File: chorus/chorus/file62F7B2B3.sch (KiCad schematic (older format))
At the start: 14 parts, among them J2 ISP, U1 LM13700, U3 ATTINY85

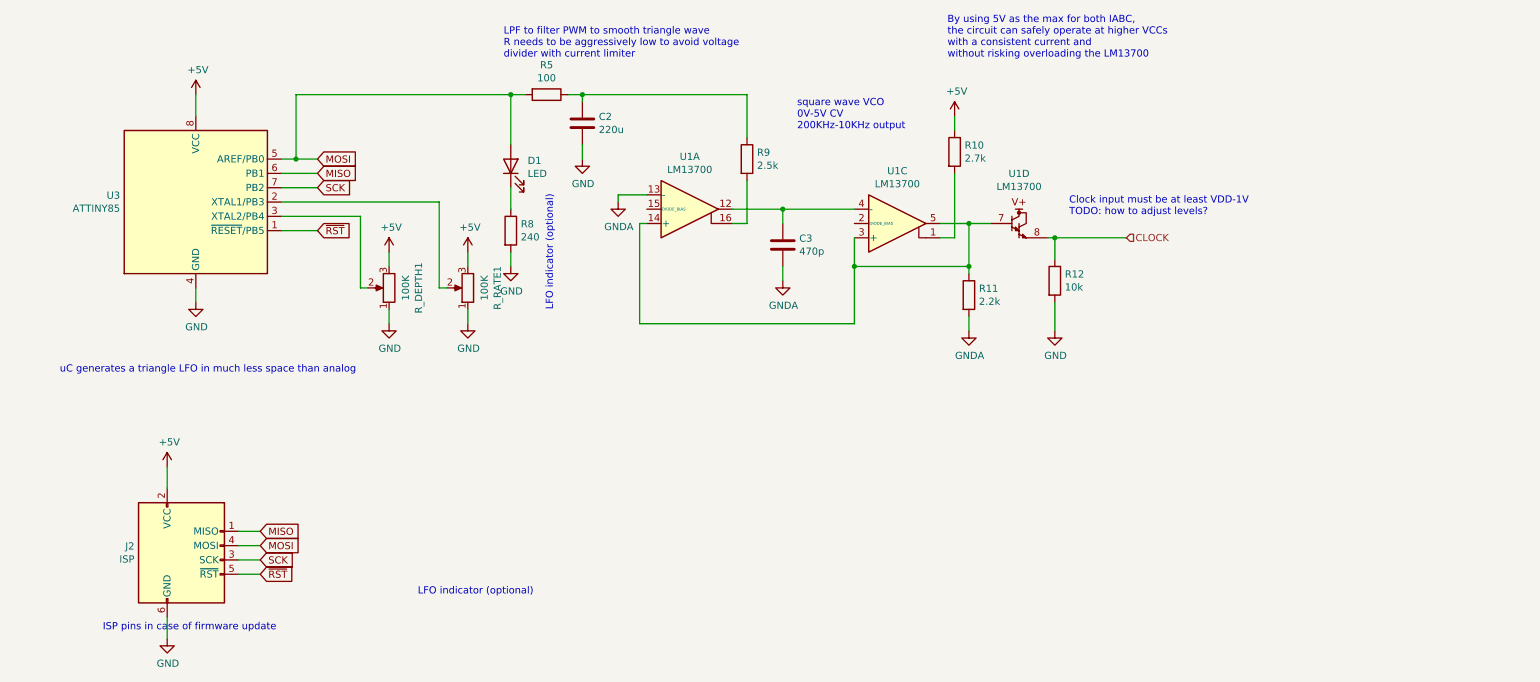
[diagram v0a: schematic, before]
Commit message: add wet/dry mix and recalculate filters
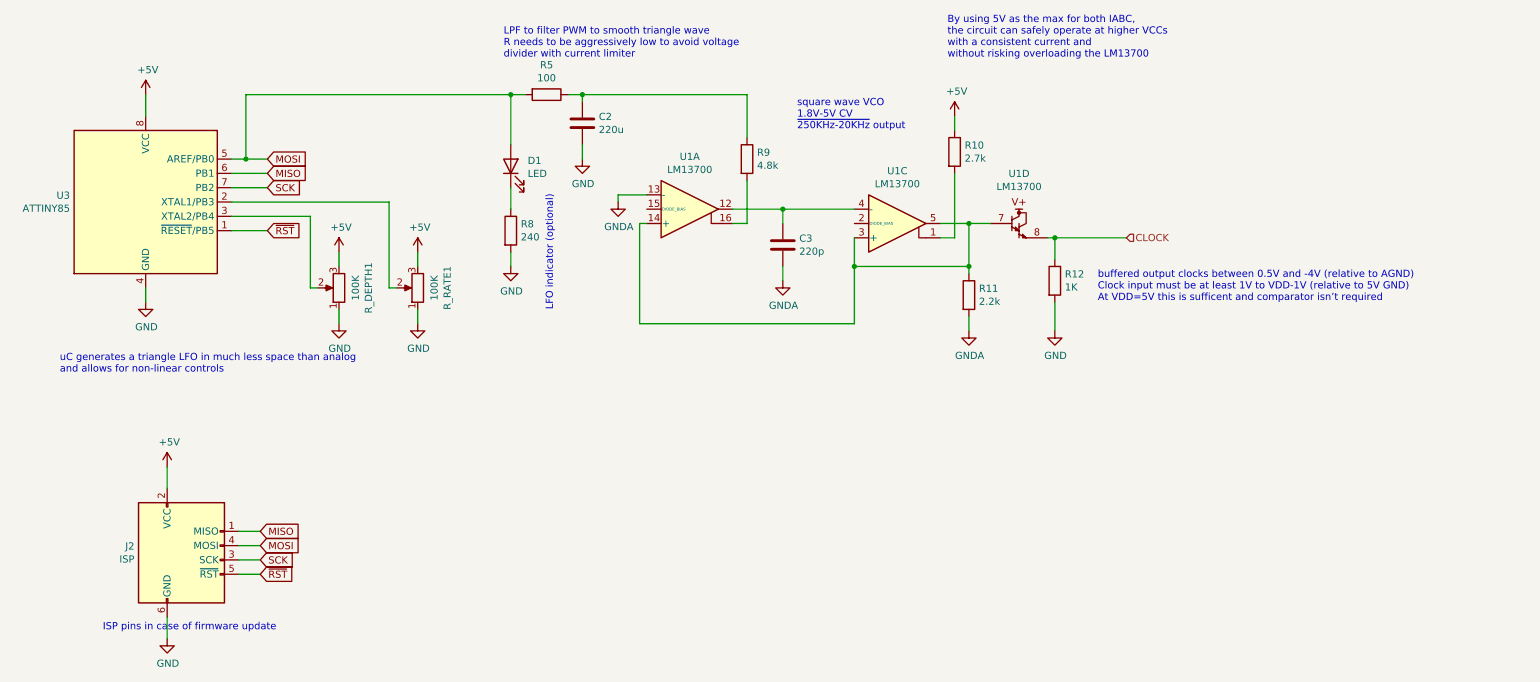
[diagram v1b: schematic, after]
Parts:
- C3: value 470p -> 220p
- R12: value 10k -> 1K
- R9: value 2.5k -> 4.8k
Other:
- note added: "buffered output clocks between 0.5V and -4V (relative to AGND)\nClock input must be at least 1V to VDD-1V (relative to 5V GND)\nAt VDD=5V this is sufficent and comparator isn’t required"
- note added: "square wave VCO\n1.8V-5V CV\n~250KHz-20KHz output"
- note added: "uC generates a triangle LFO in much less space than analog\nand allows for non-linear controls"
- note removed: "Clock input must be at least VDD-1V\nTODO: how to adjust levels?"
- note removed: "square wave VCO\n0V-5V CV\n200KHz-10KHz output"
- note removed: "uC generates a triangle LFO in much less space than analog"
- moved on the sheet: R_DEPTH1, R_RATE1, U3
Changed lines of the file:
@@
 $Descr A4 11693 8268
 encoding utf-8
-Sheet 4 6
+Sheet 3 6
 Title ""
 Date ""
@@
 L MCU_Microchip_ATtiny:ATtiny85-20PU U?
 U 1 1 62F9D27C
-P 1750 3600
+P 1400 3600
 AR Path="/62F9D27C" Ref="U?"  Part="1"
 AR Path="/62F7B2B4/62F9D27C" Ref="U3"  Part="1"
-F 0 "U3" H 1221 3646 50  0000 R CNN
-F 1 "ATTINY85" H 1221 3555 50  0000 R CNN
-F 2 "Package_DIP:DIP-8_W7.62mm" H 1750 3600 50  0001 C CIN
-F 3 "http://www.ti.com/lit/ds/symlink/tl071.pdf" H 1750 3600 50  0001 C CNN
-	1    1750 3600
+F 0 "U3" H 871 3646 50  0000 R CNN
+F 1 "ATTINY85" H 871 3555 50  0000 R CNN
+F 2 "Package_DIP:DIP-8_W7.62mm" H 1400 3600 50  0001 C CIN
+F 3 "http://www.ti.com/lit/ds/symlink/tl071.pdf" H 1400 3600 50  0001 C CNN
+	1    1400 3600
 	1    0    0    -1
 $EndComp
@@
 L power:GND #PWR?
 U 1 1 62F9D282
-P 1750 4300
+P 1400 4300
 AR Path="/62F9D282" Ref="#PWR?"  Part="1"
 AR Path="/62F7B2B4/62F9D282" Ref="#PWR0113"  Part="1"
-F 0 "#PWR0113" H 1750 4050 50  0001 C CNN
-F 1 "GND" H 1755 4127 50  0000 C CNN
-F 2 "" H 1750 4300 50  0001 C CNN
-F 3 "" H 1750 4300 50  0001 C CNN
-	1    1750 4300
-	1    0    0    -1
-$EndComp
-Wire Wire Line
-	1750 4300 1750 4200
+F 0 "#PWR0113" H 1400 4050 50  0001 C CNN
+F 1 "GND" H 1405 4127 50  0000 C CNN
+F 2 "" H 1400 4300 50  0001 C CNN
+F 3 "" H 1400 4300 50  0001 C CNN
+	1    1400 4300
+	1    0    0    -1
+$EndComp
+Wire Wire Line
+	1400 4300 1400 4200
 $Comp
 L Device:R_POT R_DEPTH?
 U 1 1 62F9D296
-P 3100 4200
+P 2750 4200
 AR Path="/62F9D296" Ref="R_DEPTH?"  Part="1"
 AR Path="/62F7B2B4/62F9D296" Ref="R_DEPTH1"  Part="1"
-F 0 "R_DEPTH1" V 2893 4200 50  0000 C CNN
-F 1 "100K" V 2984 4200 50  0000 C CNN
-F 2 "Potentiometer_THT:Potentiometer_Alps_RK09K_Single_Vertical" H 3100 4200 50  0001 C CNN
-F 3 "~" H 3100 4200 50  0001 C CNN
-	1    3100 4200
+F 0 "R_DEPTH1" V 2543 4200 50  0000 C CNN
+F 1 "100K" V 2634 4200 50  0000 C CNN
+F 2 "Potentiometer_THT:Potentiometer_Alps_RK09K_Single_Vertical" H 2750 4200 50  0001 C CNN
+F 3 "~" H 2750 4200 50  0001 C CNN
+	1    2750 4200
 	-1   0    0    1
 $EndComp
@@
 L power:GND #PWR?
 U 1 1 62F9D29C
-P 3100 4450
+P 2750 4450
 AR Path="/62F9D29C" Ref="#PWR?"  Part="1"
 AR Path="/62F7B2B4/62F9D29C" Ref="#PWR0122"  Part="1"
-F 0 "#PWR0122" H 3100 4200 50  0001 C CNN
-F 1 "GND" H 3105 4277 50  0000 C CNN
-F 2 "" H 3100 4450 50  0001 C CNN
-F 3 "" H 3100 4450 50  0001 C CNN
-	1    3100 4450
-	1    0    0    -1
-$EndComp
-Wire Wire Line
-	3100 4450 3100 4350
-Wire Wire Line
-	1750 2850 1750 3000
-Wire Wire Line
-	3100 3950 3100 4050
+F 0 "#PWR0122" H 2750 4200 50  0001 C CNN
+F 1 "GND" H 2755 4277 50  0000 C CNN
+F 2 "" H 2750 4450 50  0001 C CNN
+F 3 "" H 2750 4450 50  0001 C CNN
+	1    2750 4450
+	1    0    0    -1
+$EndComp
+Wire Wire Line
+	2750 4450 2750 4350
+Wire Wire Line
+	1400 2850 1400 3000
+Wire Wire Line
+	2750 3950 2750 4050
 $Comp
 L Connector:AVR-ISP-6 J?
@@
 Wire Wire Line
 	1550 6650 1550 6500
-Text GLabel 2600 3300 2    50   Input ~ 0
+Text GLabel 2250 3300 2    50   Input ~ 0
 MOSI
-Text GLabel 2600 3400 2    50   Input ~ 0
+Text GLabel 2250 3400 2    50   Input ~ 0
 MISO
-Text GLabel 2600 3500 2    50   Input ~ 0
+Text GLabel 2250 3500 2    50   Input ~ 0
 SCK
 Text GLabel 2200 6100 2    50   Input ~ 0
@@
 Wire Wire Line
 	2200 6200 2050 6200
-Text GLabel 2600 3800 2    50   Input ~ 0
+Text GLabel 2250 3800 2    50   Input ~ 0
 ~RST
 Wire Wire Line
-	2950 4200 2900 4200
-Wire Wire Line
-	2900 4200 2900 3700
+	2600 4200 2550 4200
+Wire Wire Line
+	2550 4200 2550 3700
 Text Notes 800  4800 0    50   ~ 0
-uC generates a triangle LFO in much less space than analog
+uC generates a triangle LFO in much less space than analog\nand allows for non-linear controls
 $Comp
 L power:+5V #PWR?
@@
 L power:+5V #PWR?
 U 1 1 62F9D2CB
-P 1750 2850
+P 1400 2850
 AR Path="/62F9D2CB" Ref="#PWR?"  Part="1"
 AR Path="/62F7B2B4/62F9D2CB" Ref="#PWR0125"  Part="1"
-F 0 "#PWR0125" H 1750 2700 50  0001 C CNN
-F 1 "+5V" H 1765 3023 50  0000 C CNN
-F 2 "" H 1750 2850 50  0001 C CNN
-F 3 "" H 1750 2850 50  0001 C CNN
-	1    1750 2850
+F 0 "#PWR0125" H 1400 2700 50  0001 C CNN
+F 1 "+5V" H 1415 3023 50  0000 C CNN
+F 2 "" H 1400 2850 50  0001 C CNN
+F 3 "" H 1400 2850 50  0001 C CNN
+	1    1400 2850
 	1    0    0    -1
 $EndComp
@@
 L power:+5V #PWR?
 U 1 1 62F9D2D2
-P 3100 3950
+P 2750 3950
 AR Path="/62F9D2D2" Ref="#PWR?"  Part="1"
 AR Path="/62F7B2B4/62F9D2D2" Ref="#PWR0126"  Part="1"
-F 0 "#PWR0126" H 3100 3800 50  0001 C CNN
-F 1 "+5V" H 3115 4123 50  0000 C CNN
-F 2 "" H 3100 3950 50  0001 C CNN
-F 3 "" H 3100 3950 50  0001 C CNN
-	1    3100 3950
-	1    0    0    -1
-$EndComp
-Text Notes 7850 3700 0    50   ~ 0
-Clock input must be at least VDD-1V\nTODO: how to adjust levels?
+F 0 "#PWR0126" H 2750 3800 50  0001 C CNN
+F 1 "+5V" H 2765 4123 50  0000 C CNN
+F 2 "" H 2750 3950 50  0001 C CNN
+F 3 "" H 2750 3950 50  0001 C CNN
+	1    2750 3950
+	1    0    0    -1
+$EndComp
+Text Notes 8050 4300 0    50   ~ 0
+buffered output clocks between 0.5V and -4V (relative to AGND)\nClock input must be at least 1V to VDD-1V (relative to 5V GND)\nAt VDD=5V this is sufficent and comparator isn’t required
 $Comp
 L Amplifier_Operational:LM13700 U?
@@
 AR Path="/62F7B2B4/62F9D2F1" Ref="C3"  Part="1"
 F 0 "C3" H 5965 3946 50  0000 L CNN
-F 1 "470p" H 5965 3855 50  0000 L CNN
+F 1 "220p" H 5965 3855 50  0000 L CNN
 F 2 "Capacitor_THT:C_Disc_D6.0mm_W2.5mm_P5.00mm" H 5888 3750 50  0001 C CNN
 F 3 "~" H 5850 3900 50  0001 C CNN
@@
 AR Path="/62F7B2B4/62F9D31A" Ref="R12"  Part="1"
 F 0 "R12" H 7820 4196 50  0000 L CNN
-F 1 "10k" H 7820 4105 50  0000 L CNN
+F 1 "1K" H 7820 4105 50  0000 L CNN
 F 2 "Resistor_THT:R_Axial_DIN0204_L3.6mm_D1.6mm_P2.54mm_Vertical" V 7680 4150 50  0001 C CNN
 F 3 "~" H 7750 4150 50  0001 C CNN
@@
 AR Path="/62F7B2B4/62F9D356" Ref="R9"  Part="1"
 F 0 "R9" H 5670 3346 50  0000 L CNN
-F 1 "2.5k" H 5670 3255 50  0000 L CNN
+F 1 "4.8k" H 5670 3255 50  0000 L CNN
 F 2 "Resistor_THT:R_Axial_DIN0204_L3.6mm_D1.6mm_P2.54mm_Vertical" V 5530 3300 50  0001 C CNN
 F 3 "~" H 5600 3300 50  0001 C CNN
@@
 	5600 3750 5500 3750
 Text Notes 5950 3100 0    50   ~ 0
-square wave VCO\n0V-5V CV\n200KHz-10KHz output
-Wire Wire Line
-	2350 3500 2600 3500
-Wire Wire Line
-	2600 3800 2350 3800
-Wire Wire Line
-	2900 3700 2350 3700
+square wave VCO\n1.8V-5V CV\n~250KHz-20KHz output
+Wire Wire Line
+	2000 3500 2250 3500
+Wire Wire Line
+	2250 3800 2000 3800
+Wire Wire Line
+	2550 3700 2000 3700
 Text HLabel 8250 3850 2    50   Input ~ 0
 CLOCK
@@
 Wire Wire Line
 	3950 3650 3950 3500
-Text Notes 3300 6350 0    50   ~ 0
-LFO indicator (optional)
 $Comp
 L power:+5V #PWR?
@@
 L Device:R_POT R_RATE?
 U 1 1 62F9D289
-P 3650 4200
+P 3300 4200
 AR Path="/62F9D289" Ref="R_RATE?"  Part="1"
 AR Path="/62F7B2B4/62F9D289" Ref="R_RATE1"  Part="1"
-F 0 "R_RATE1" V 3443 4200 50  0000 C CNN
-F 1 "100K" V 3534 4200 50  0000 C CNN
-F 2 "Potentiometer_THT:Potentiometer_Alps_RK09K_Single_Vertical" H 3650 4200 50  0001 C CNN
-F 3 "~" H 3650 4200 50  0001 C CNN
-	1    3650 4200
+F 0 "R_RATE1" V 3093 4200 50  0000 C CNN
+F 1 "100K" V 3184 4200 50  0000 C CNN
+F 2 "Potentiometer_THT:Potentiometer_Alps_RK09K_Single_Vertical" H 3300 4200 50  0001 C CNN
+F 3 "~" H 3300 4200 50  0001 C CNN
+	1    3300 4200
 	-1   0    0    1
 $EndComp
 Wire Wire Line
-	3650 3950 3650 4050
-Wire Wire Line
-	3650 4450 3650 4350
+	3300 3950 3300 4050
+Wire Wire Line
+	3300 4450 3300 4350
 $Comp
 L power:GND #PWR?
 U 1 1 62F9D28F
-P 3650 4450
+P 3300 4450
 AR Path="/62F9D28F" Ref="#PWR?"  Part="1"
 AR Path="/62F7B2B4/62F9D28F" Ref="#PWR0121"  Part="1"
-F 0 "#PWR0121" H 3650 4200 50  0001 C CNN
-F 1 "GND" H 3655 4277 50  0000 C CNN
-F 2 "" H 3650 4450 50  0001 C CNN
-F 3 "" H 3650 4450 50  0001 C CNN
-	1    3650 4450
+F 0 "#PWR0121" H 3300 4200 50  0001 C CNN
+F 1 "GND" H 3305 4277 50  0000 C CNN
+F 2 "" H 3300 4450 50  0001 C CNN
+F 3 "" H 3300 4450 50  0001 C CNN
+	1    3300 4450
 	1    0    0    -1
 $EndComp
@@
 L power:+5V #PWR?
 U 1 1 62F9D2D8
-P 3650 3950
+P 3300 3950
 AR Path="/62F9D2D8" Ref="#PWR?"  Part="1"
 AR Path="/62F7B2B4/62F9D2D8" Ref="#PWR0127"  Part="1"
-F 0 "#PWR0127" H 3650 3800 50  0001 C CNN
-F 1 "+5V" H 3665 4123 50  0000 C CNN
-F 2 "" H 3650 3950 50  0001 C CNN
-F 3 "" H 3650 3950 50  0001 C CNN
-	1    3650 3950
-	1    0    0    -1
-$EndComp
-Wire Wire Line
-	3450 3600 2350 3600
-Wire Wire Line
-	3500 4200 3450 4200
-Wire Wire Line
-	3450 4200 3450 3600
-Wire Wire Line
-	2350 3300 2450 3300
-Wire Wire Line
-	2600 3400 2350 3400
-Connection ~ 2450 3300
-Wire Wire Line
-	2450 3300 2600 3300
+F 0 "#PWR0127" H 3300 3800 50  0001 C CNN
+F 1 "+5V" H 3315 4123 50  0000 C CNN
+F 2 "" H 3300 3950 50  0001 C CNN
+F 3 "" H 3300 3950 50  0001 C CNN
+	1    3300 3950
+	1    0    0    -1
+$EndComp
+Wire Wire Line
+	3100 3600 2000 3600
+Wire Wire Line
+	3150 4200 3100 4200
+Wire Wire Line
+	3100 4200 3100 3600
+Wire Wire Line
+	2000 3300 2100 3300
+Wire Wire Line
+	2250 3400 2000 3400
+Connection ~ 2100 3300
+Wire Wire Line
+	2100 3300 2250 3300
 Wire Wire Line
 	4450 2850 5600 2850
@@
 	4050 2850 3950 2850
 Wire Wire Line
-	2450 2850 2450 3300
+	2100 2850 2100 3300
 Wire Wire Line
 	3950 2850 3950 3200
-Connection ~ 3950 2850
-Wire Wire Line
-	3950 2850 2450 2850
 $Comp
 L power:GND #PWR?
@@
 Text Notes 3900 2600 0    50   ~ 0
 LPF to filter PWM to smooth triangle wave\nR needs to be aggressively low to avoid voltage\ndivider with current limiter
+Wire Wire Line
+	2100 2850 3950 2850
+Connection ~ 3950 2850
 $EndSCHEMATC

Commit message: assembled psu and clock
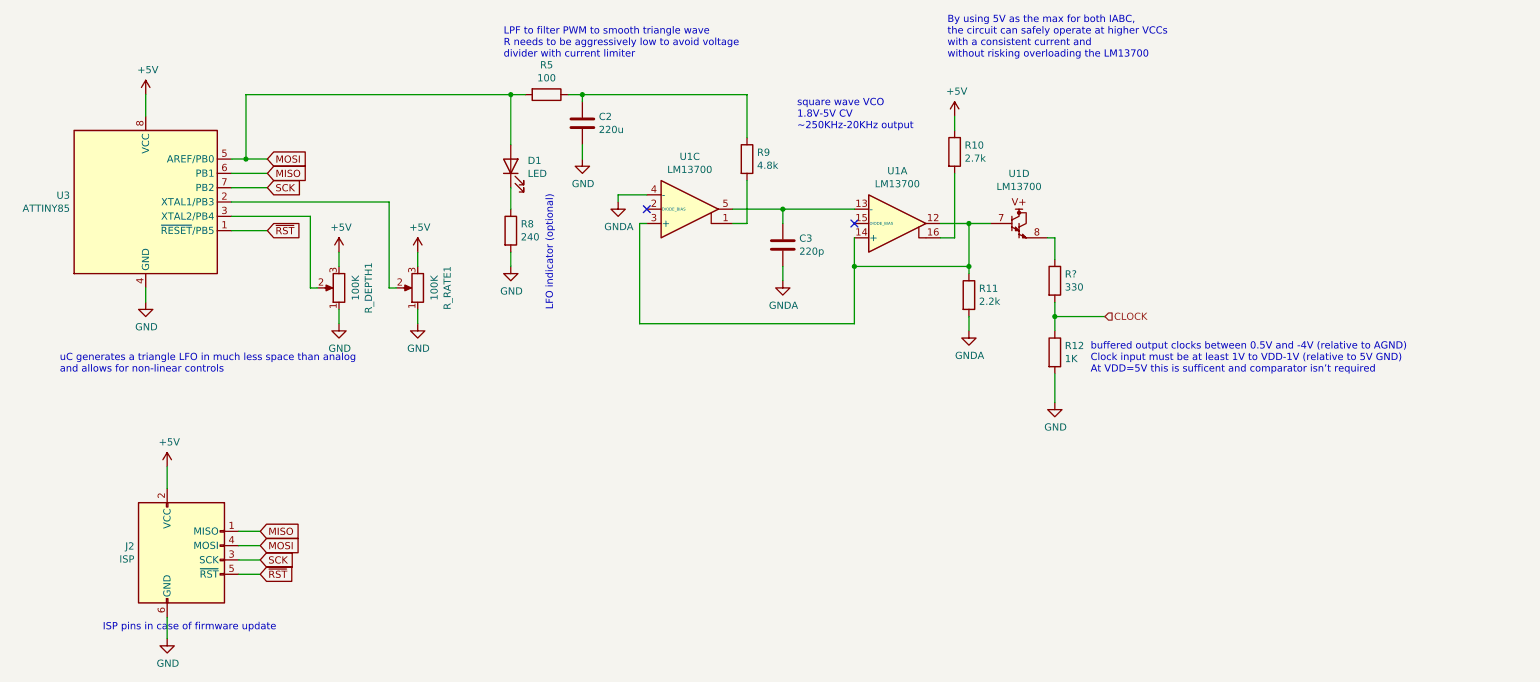
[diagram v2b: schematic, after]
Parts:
- added R?: 330, Resistor_THT:R_Axial_DIN0204_L3.6mm_D1.6mm_P2.54mm_Vertical, symbol Device:R
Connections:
- net CLOCK: now also R?.2; no longer U1.8
- net GNDA: now also U1.4 (-); no longer U1.13 (-)
- net at R11.1, U1.14 (+), U1.3 (+)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: now also U1.12; no longer U1.5
- net at U1.16: now also R10.2; no longer R9.2
- net at U1.1: now also R9.2; no longer R10.2
- new net: R?.1, U1.8
- new net: C3.1, U1.13 (-), U1.5
- no-connect marks 0 -> 2
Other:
- note added: "square wave VCO\n1.8V-5V CV\n~~250KHz-20KHz output"
- note removed: "square wave VCO\n1.8V-5V CV\n~250KHz-20KHz output"
- moved on the sheet: R12, U1A, U1C
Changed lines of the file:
@@
 	1    0    0    -1
 $EndComp
-Text Notes 8050 4300 0    50   ~ 0
+Text Notes 8000 4800 0    50   ~ 0
 buffered output clocks between 0.5V and -4V (relative to AGND)\nClock input must be at least 1V to VDD-1V (relative to 5V GND)\nAt VDD=5V this is sufficent and comparator isn’t required
-$Comp
-L Amplifier_Operational:LM13700 U?
-U 1 1 62F9D2DF
-P 5200 3650
-AR Path="/62F9D2DF" Ref="U?"  Part="1"
-AR Path="/62F7B2B4/62F9D2DF" Ref="U1"  Part="1"
-F 0 "U1" H 5200 4017 50  0000 C CNN
-F 1 "LM13700" H 5200 3926 50  0000 C CNN
-F 2 "Package_DIP:DIP-16_W7.62mm" H 4900 3675 50  0001 C CNN
-F 3 "http://www.ti.com/lit/ds/symlink/lm13700.pdf" H 4900 3675 50  0001 C CNN
-	1    5200 3650
-	1    0    0    -1
-$EndComp
-$Comp
-L Amplifier_Operational:LM13700 U?
-U 3 1 62F9D2E5
-P 6650 3750
-AR Path="/62F9D2E5" Ref="U?"  Part="3"
-AR Path="/62F7B2B4/62F9D2E5" Ref="U1"  Part="3"
-F 0 "U1" H 6650 4117 50  0000 C CNN
-F 1 "LM13700" H 6650 4026 50  0000 C CNN
-F 2 "Package_DIP:DIP-16_W7.62mm" H 6350 3775 50  0001 C CNN
-F 3 "http://www.ti.com/lit/ds/symlink/lm13700.pdf" H 6350 3775 50  0001 C CNN
-	3    6650 3750
-	1    0    0    -1
-$EndComp
 $Comp
 L power:GNDA #PWR?
@@
 	7150 4400 7150 4500
 $Comp
-L Amplifier_Operational:LM13700 U?
-U 4 1 62F9D314
-P 7600 3750
-AR Path="/62F9D314" Ref="U?"  Part="4"
-AR Path="/62F7B2B4/62F9D314" Ref="U1"  Part="4"
-F 0 "U1" H 7500 4098 50  0000 C CNN
-F 1 "LM13700" H 7500 4007 50  0000 C CNN
-F 2 "Package_DIP:DIP-16_W7.62mm" H 7300 3775 50  0001 C CNN
-F 3 "http://www.ti.com/lit/ds/symlink/lm13700.pdf" H 7300 3775 50  0001 C CNN
-	4    7600 3750
-	1    0    0    -1
-$EndComp
-$Comp
 L Device:R R?
 U 1 1 62F9D31A
-P 7750 4150
+P 7750 4650
 AR Path="/62F9D31A" Ref="R?"  Part="1"
 AR Path="/62F7B2B4/62F9D31A" Ref="R12"  Part="1"
-F 0 "R12" H 7820 4196 50  0000 L CNN
-F 1 "1K" H 7820 4105 50  0000 L CNN
-F 2 "Resistor_THT:R_Axial_DIN0204_L3.6mm_D1.6mm_P2.54mm_Vertical" V 7680 4150 50  0001 C CNN
-F 3 "~" H 7750 4150 50  0001 C CNN
-	1    7750 4150
+F 0 "R12" H 7820 4696 50  0000 L CNN
+F 1 "1K" H 7820 4605 50  0000 L CNN
+F 2 "Resistor_THT:R_Axial_DIN0204_L3.6mm_D1.6mm_P2.54mm_Vertical" V 7680 4650 50  0001 C CNN
+F 3 "~" H 7750 4650 50  0001 C CNN
+	1    7750 4650
 	1    0    0    -1
 $EndComp
@@
 L power:GND #PWR?
 U 1 1 62F9D320
-P 7750 4500
+P 7750 5000
 AR Path="/62F9D320" Ref="#PWR?"  Part="1"
 AR Path="/62F7B2B4/62F9D320" Ref="#PWR0131"  Part="1"
-F 0 "#PWR0131" H 7750 4250 50  0001 C CNN
-F 1 "GND" H 7755 4327 50  0000 C CNN
-F 2 "" H 7750 4500 50  0001 C CNN
-F 3 "" H 7750 4500 50  0001 C CNN
-	1    7750 4500
-	1    0    0    -1
-$EndComp
-Wire Wire Line
-	7750 4500 7750 4300
+F 0 "#PWR0131" H 7750 4750 50  0001 C CNN
+F 1 "GND" H 7755 4827 50  0000 C CNN
+F 2 "" H 7750 5000 50  0001 C CNN
+F 3 "" H 7750 5000 50  0001 C CNN
+	1    7750 5000
+	1    0    0    -1
+$EndComp
+Wire Wire Line
+	7750 5000 7750 4800
 Wire Wire Line
 	7750 4000 7750 3850
@@
 	5600 3750 5500 3750
 Text Notes 5950 3100 0    50   ~ 0
-square wave VCO\n1.8V-5V CV\n~250KHz-20KHz output
+square wave VCO\n1.8V-5V CV\n~~250KHz-20KHz output
 Wire Wire Line
 	2000 3500 2250 3500
@@
 Wire Wire Line
 	2550 3700 2000 3700
-Text HLabel 8250 3850 2    50   Input ~ 0
+Text HLabel 8100 4400 2    50   Input ~ 0
 CLOCK
 Wire Wire Line
 	7700 3850 7750 3850
-Connection ~ 7750 3850
-Wire Wire Line
-	7750 3850 8250 3850
 $Comp
 L Device:LED D?
@@
 	2100 2850 3950 2850
 Connection ~ 3950 2850
+NoConn ~ 6350 3750
+NoConn ~ 4900 3650
+$Comp
+L Amplifier_Operational:LM13700 U?
+U 3 1 62F9D2E5
+P 5200 3650
+AR Path="/62F9D2E5" Ref="U?"  Part="3"
+AR Path="/62F7B2B4/62F9D2E5" Ref="U1"  Part="3"
+F 0 "U1" H 5200 4017 50  0000 C CNN
+F 1 "LM13700" H 5200 3926 50  0000 C CNN
+F 2 "Package_DIP:DIP-16_W7.62mm" H 4900 3675 50  0001 C CNN
+F 3 "http://www.ti.com/lit/ds/symlink/lm13700.pdf" H 4900 3675 50  0001 C CNN
+	3    5200 3650
+	1    0    0    -1
+$EndComp
+$Comp
+L Amplifier_Operational:LM13700 U?
+U 1 1 62F9D2DF
+P 6650 3750
+AR Path="/62F9D2DF" Ref="U?"  Part="1"
+AR Path="/62F7B2B4/62F9D2DF" Ref="U1"  Part="1"
+F 0 "U1" H 6650 4117 50  0000 C CNN
+F 1 "LM13700" H 6650 4026 50  0000 C CNN
+F 2 "Package_DIP:DIP-16_W7.62mm" H 6350 3775 50  0001 C CNN
+F 3 "http://www.ti.com/lit/ds/symlink/lm13700.pdf" H 6350 3775 50  0001 C CNN
+	1    6650 3750
+	1    0    0    -1
+$EndComp
+$Comp
+L Amplifier_Operational:LM13700 U?
+U 4 1 62F9D314
+P 7600 3750
+AR Path="/62F9D314" Ref="U?"  Part="4"
+AR Path="/62F7B2B4/62F9D314" Ref="U1"  Part="4"
+F 0 "U1" H 7500 4098 50  0000 C CNN
+F 1 "LM13700" H 7500 4007 50  0000 C CNN
+F 2 "Package_DIP:DIP-16_W7.62mm" H 7300 3775 50  0001 C CNN
+F 3 "http://www.ti.com/lit/ds/symlink/lm13700.pdf" H 7300 3775 50  0001 C CNN
+	4    7600 3750
+	1    0    0    -1
+$EndComp
+$Comp
+L Device:R R?
+U 1 1 62AF3015
+P 7750 4150
+AR Path="/62AF3015" Ref="R?"  Part="1"
+AR Path="/62F7B2B4/62AF3015" Ref="R?"  Part="1"
+F 0 "R?" H 7820 4196 50  0000 L CNN
+F 1 "330" H 7820 4105 50  0000 L CNN
+F 2 "Resistor_THT:R_Axial_DIN0204_L3.6mm_D1.6mm_P2.54mm_Vertical" V 7680 4150 50  0001 C CNN
+F 3 "~" H 7750 4150 50  0001 C CNN
+	1    7750 4150
+	1    0    0    -1
+$EndComp
+Wire Wire Line
+	7750 4500 7750 4400
+Wire Wire Line
+	8100 4400 7750 4400
+Connection ~ 7750 4400
+Wire Wire Line
+	7750 4400 7750 4300
 $EndSCHEMATC
